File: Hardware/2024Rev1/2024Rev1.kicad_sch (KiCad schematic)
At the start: 87 parts, among them J7 RJ45_LED_Shielded, Q2 BSS138, Q3 BSS138, Q5 BSS138, Q6 SPD30P06PGBTMA1, Q7 BSS138, U2 Opamp_Dual, U3 Teensy4.1_DEV-16771, U4 Opamp_Dual, U5 Opamp_Dual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

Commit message: rearranged flags
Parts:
- removed Conn2: AndersonPP, MRDT_Connectors:Square_Anderson_2_V_Side_By_Side, symbol MRDT_Connectors:AndersonPP
- removed D8: Green, LED_SMD:LED_0603_1608Metric_Pad1.05x0.95mm_HandSolder, symbol Device:LED
- removed R49: 3K, Resistor_SMD:R_0603_1608Metric_Pad0.98x0.95mm_HandSolder, symbol Device:R
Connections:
- net Gate is gone; now on net Cell4-SENSE: U3.41 (A17)
- net Buzzer-Teensy: now also U3.4 (BCLK2); no longer U3.25 (A11)
- net CURRENT_SENSE: now also U3.21 (A7); no longer U3.27 (A13)
- net Cell1-SENSE: now also U3.17 (A3); no longer U3.14 (A0)
- net Cell2-SENSE: now also U3.18 (A4); no longer U3.15 (A1)
- net Cell3-SENSE: now also U3.40 (A16); no longer U3.16 (A2)
- net Cell4-SENSE: no longer U3.17 (A3)
- net Cell5-SENSE: now also U3.38 (A14); no longer U3.18 (A4)
- net Cell6-SENSE: now also U3.39 (A15); no longer U3.19 (A5)
- net Cell7-SENSE: now also U3.25 (A11); no longer U3.20 (A6)
- net Cell8-SENSE: now also U3.24 (A10); no longer U3.21 (A7)
- net ERR_LED: now also U3.34 (RX8); no longer U3.38 (A14)
- net Fan-Teensy: now also U3.23 (A9); no longer U3.26 (A12)
- net GATE: now also U3.33 (MCLK2)
- net LCD_TX: now also U3.20 (A6); no longer U3.1 (TX1)
- net LOGIC_SWITCH_INPUT: now also U3.22 (A8); no longer U3.40 (A16)
- net TempSensor: now also U3.16 (A2); no longer U3.24 (A10)
- no-connect marks 37 -> 35

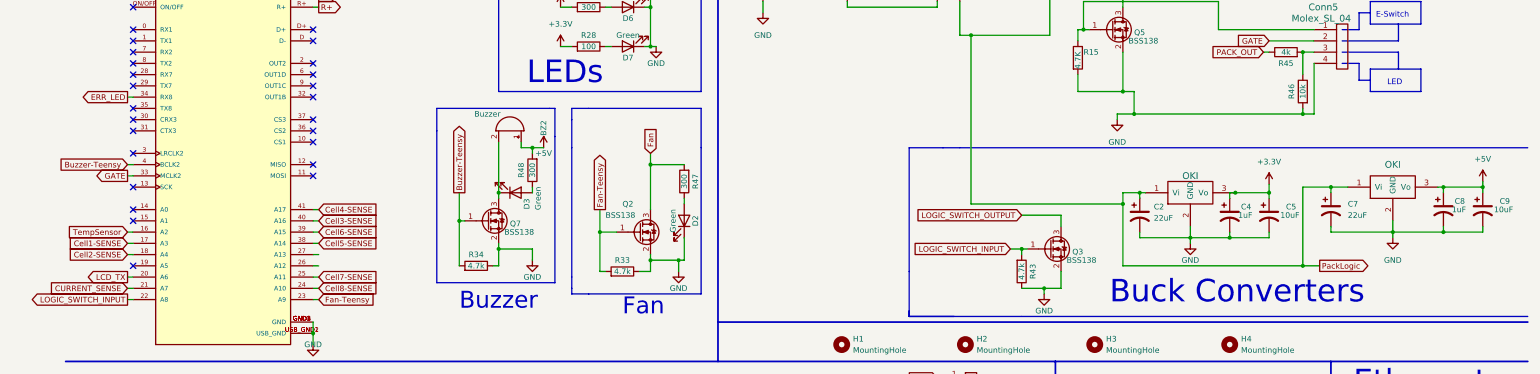
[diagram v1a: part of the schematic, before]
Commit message: polished components placement
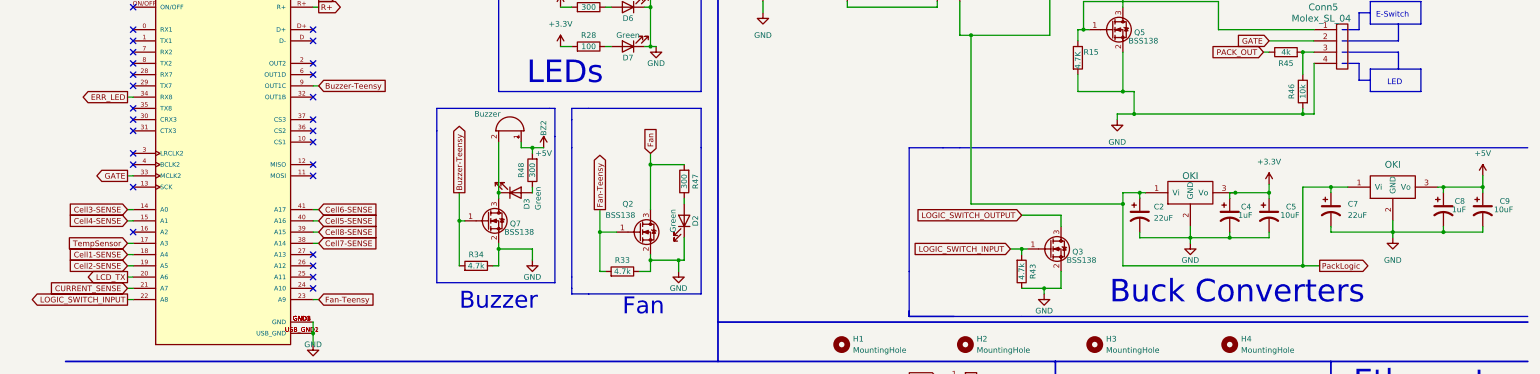
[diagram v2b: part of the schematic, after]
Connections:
- net Buzzer-Teensy: now also U3.9 (OUT1C); no longer U3.4 (BCLK2)
- net Cell1-SENSE: now also U3.18 (A4); no longer U3.17 (A3)
- net Cell2-SENSE: now also U3.19 (A5); no longer U3.18 (A4)
- net Cell3-SENSE: now also U3.14 (A0); no longer U3.40 (A16)
- net Cell4-SENSE: now also U3.15 (A1); no longer U3.41 (A17)
- net Cell5-SENSE: now also U3.40 (A16); no longer U3.38 (A14)
- net Cell6-SENSE: now also U3.41 (A17); no longer U3.39 (A15)
- net Cell7-SENSE: now also U3.38 (A14); no longer U3.25 (A11)
- net Cell8-SENSE: now also U3.39 (A15); no longer U3.24 (A10)
- net TempSensor: now also U3.17 (A3); no longer U3.16 (A2)
- no-connect marks 35 -> 37
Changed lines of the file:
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@@
   (no_connect (at 68.58 64.77))
   (no_connect (at 68.58 59.69))
-  (no_connect (at 68.58 57.15))
   (no_connect (at 68.58 54.61))
   (no_connect (at 68.58 52.07))
@@
   (no_connect (at 27.94 80.01))
   (no_connect (at 68.58 16.51))
+  (no_connect (at 68.58 102.87))
   (no_connect (at 327.66 153.67))
+  (no_connect (at 68.58 95.25))
   (no_connect (at 27.94 46.99))
-  (no_connect (at 27.94 97.79))
-  (no_connect (at 27.94 85.09))
+  (no_connect (at 68.58 100.33))
+  (no_connect (at 27.94 74.93))
   (no_connect (at 68.58 19.05))
+  (no_connect (at 68.58 97.79))
   (no_connect (at 68.58 44.45))
   (no_connect (at 68.58 46.99))
   (no_connect (at 314.96 133.35))
-  (no_connect (at 27.94 87.63))
+  (no_connect (at 27.94 90.17))
   (polyline (pts (xy 300.99 52.07) (xy 304.8 52.07))
     (stroke (width 0) (type default))
   )
+  (wire (pts (xy 26.67 87.63) (xy 27.94 87.63))
+    (stroke (width 0) (type default))
+  )
   (wire (pts (xy 31.75 138.176) (xy 32.004 138.176))
     (stroke (width 0) (type default))
@@
     (stroke (width 0) (type default))
   )
-  (wire (pts (xy 26.67 90.17) (xy 27.94 90.17))
-    (stroke (width 0) (type default))
-  )
   (wire (pts (xy 214.63 45.72) (xy 214.63 38.1))
     (stroke (width 0) (type default))
@@
     (stroke (width 0) (type default))
   )
-  (wire (pts (xy 69.85 100.33) (xy 68.58 100.33))
-    (stroke (width 0) (type default))
-  )
   (wire (pts (xy 26.67 105.41) (xy 27.94 105.41))
     (stroke (width 0) (type default))
@@
     (stroke (width 0) (type default))
   )
-  (wire (pts (xy 26.67 74.93) (xy 27.94 74.93))
-    (stroke (width 0) (type default))
-  )
   (wire (pts (xy 251.46 58.42) (xy 254 58.42))
     (stroke (width 0) (type default))
@@
     (stroke (width 0) (type default))
   )
+  (wire (pts (xy 26.67 85.09) (xy 27.94 85.09))
+    (stroke (width 0) (type default))
+  )
   (polyline (pts (xy 166.624 199.136) (xy 157.734 199.136))
     (stroke (width 0) (type default))
@@
     (stroke (width 0) (type default))
   )
+  (wire (pts (xy 69.85 57.15) (xy 68.58 57.15))
+    (stroke (width 0) (type default))
+  )
   (wire (pts (xy 71.12 165.1) (xy 71.12 168.91))
     (stroke (width 0) (type default))
@@
     (stroke (width 0) (type default))
   )
+  (wire (pts (xy 26.67 97.79) (xy 27.94 97.79))
+    (stroke (width 0) (type default))
+  )
   (polyline (pts (xy 166.624 190.246) (xy 166.624 199.136))
     (stroke (width 0) (type default))
@@
     (stroke (width 0) (type default))
   )
-  (wire (pts (xy 332.74 80.01) (xy 332.74 78.74))
+  (wire (pts (xy 332.74 80.01) (xy 332.74 77.47))
     (stroke (width 0) (type default))
   )
@@
     (stroke (width 0) (type default))
   )
-  (wire (pts (xy 69.85 102.87) (xy 68.58 102.87))
-    (stroke (width 0) (type default))
-  )
   (wire (pts (xy 241.3 44.45) (xy 241.3 46.99))
     (stroke (width 0) (type default))
@@
     (stroke (width 0) (type default))
   )
-  (wire (pts (xy 69.85 95.25) (xy 68.58 95.25))
-    (stroke (width 0) (type default))
-  )
   (wire (pts (xy 137.16 90.17) (xy 133.35 90.17))
     (stroke (width 0) (type default))
@@
     (stroke (width 0) (type default))
   )
-  (wire (pts (xy 69.85 97.79) (xy 68.58 97.79))
-    (stroke (width 0) (type default))
-  )
   (polyline (pts (xy 156.21 62.23) (xy 156.21 71.12))
     (stroke (width 0) (type default))
@@
     (effects (font (size 1.27 1.27)) (justify right bottom))
   )
-  (global_label "Cell4-SENSE" (shape input) (at 69.85 85.09 0) (fields_autoplaced)
-    (effects (font (size 1.27 1.27)) (justify left))
-    (property "Intersheetrefs" "${INTERSHEET_REFS}" (at 85.3536 85.09 0)
-      (effects (font (size 1.27 1.27)) (justify left) hide)
+  (global_label "Cell4-SENSE" (shape input) (at 26.67 87.63 180) (fields_autoplaced)
+    (effects (font (size 1.27 1.27)) (justify right))
+    (property "Intersheetrefs" "${INTERSHEET_REFS}" (at 11.1664 87.63 0)
+      (effects (font (size 1.27 1.27)) (justify right) hide)
     )
   )
@@
     )
   )
-  (global_label "Cell3-SENSE" (shape input) (at 69.85 87.63 0) (fields_autoplaced)
-    (effects (font (size 1.27 1.27)) (justify left))
-    (property "Intersheetrefs" "${INTERSHEET_REFS}" (at 85.3536 87.63 0)
-      (effects (font (size 1.27 1.27)) (justify left) hide)
+  (global_label "Cell3-SENSE" (shape input) (at 26.67 85.09 180) (fields_autoplaced)
+    (effects (font (size 1.27 1.27)) (justify right))
+    (property "Intersheetrefs" "${INTERSHEET_REFS}" (at 11.1664 85.09 0)
+      (effects (font (size 1.27 1.27)) (justify right) hide)
     )
   )
@@
     )
   )
-  (global_label "Cell6-SENSE" (shape input) (at 69.85 90.17 0) (fields_autoplaced)
+  (global_label "Cell6-SENSE" (shape input) (at 69.85 85.09 0) (fields_autoplaced)
     (effects (font (size 1.27 1.27)) (justify left))
-    (property "Intersheetrefs" "${INTERSHEET_REFS}" (at 85.3536 90.17 0)
+    (property "Intersheetrefs" "${INTERSHEET_REFS}" (at 85.3536 85.09 0)
       (effects (font (size 1.27 1.27)) (justify left) hide)
     )
@@
     )
   )
-  (global_label "Cell1-SENSE" (shape input) (at 26.67 92.71 180) (fields_autoplaced)
+  (global_label "Cell1-SENSE" (shape input) (at 26.67 95.25 180) (fields_autoplaced)
     (effects (font (size 1.27 1.27)) (justify right))
-    (property "Intersheetrefs" "${INTERSHEET_REFS}" (at 11.1664 92.71 0)
+    (property "Intersheetrefs" "${INTERSHEET_REFS}" (at 11.1664 95.25 0)
       (effects (font (size 1.27 1.27)) (justify right) hide)
     )
@@
     )
   )
-  (global_label "Cell7-SENSE" (shape input) (at 69.85 100.33 0) (fields_autoplaced)
+  (global_label "Cell7-SENSE" (shape input) (at 69.85 92.71 0) (fields_autoplaced)
     (effects (font (size 1.27 1.27)) (justify left))
-    (property "Intersheetrefs" "${INTERSHEET_REFS}" (at 85.3536 100.33 0)
+    (property "Intersheetrefs" "${INTERSHEET_REFS}" (at 85.3536 92.71 0)
       (effects (font (size 1.27 1.27)) (justify left) hide)
     )
   )
-  (global_label "TempSensor" (shape input) (at 26.67 90.17 180) (fields_autoplaced)
+  (global_label "TempSensor" (shape input) (at 26.67 92.71 180) (fields_autoplaced)
     (effects (font (size 1.27 1.27)) (justify right))
-    (property "Intersheetrefs" "${INTERSHEET_REFS}" (at 12.3759 90.17 0)
+    (property "Intersheetrefs" "${INTERSHEET_REFS}" (at 12.3759 92.71 0)
       (effects (font (size 1.27 1.27)) (justify right) hide)
     )
@@
     )
   )
-  (global_label "Buzzer-Teensy" (shape input) (at 26.67 74.93 180) (fields_autoplaced)
-    (effects (font (size 1.27 1.27)) (justify right))
-    (property "Intersheetrefs" "${INTERSHEET_REFS}" (at 9.4729 74.93 0)
-      (effects (font (size 1.27 1.27)) (justify right) hide)
+  (global_label "Buzzer-Teensy" (shape input) (at 69.85 57.15 0) (fields_autoplaced)
+    (effects (font (size 1.27 1.27)) (justify left))
+    (property "Intersheetrefs" "${INTERSHEET_REFS}" (at 87.0471 57.15 0)
+      (effects (font (size 1.27 1.27)) (justify left) hide)
     )
   )
@@
     )
   )
-  (global_label "Cell2-SENSE" (shape input) (at 26.67 95.25 180) (fields_autoplaced)
+  (global_label "Cell2-SENSE" (shape input) (at 26.67 97.79 180) (fields_autoplaced)
     (effects (font (size 1.27 1.27)) (justify right))
-    (property "Intersheetrefs" "${INTERSHEET_REFS}" (at 11.1664 95.25 0)
+    (property "Intersheetrefs" "${INTERSHEET_REFS}" (at 11.1664 97.79 0)
       (effects (font (size 1.27 1.27)) (justify right) hide)
     )
@@
     )
   )
-  (global_label "Cell8-SENSE" (shape input) (at 69.85 102.87 0) (fields_autoplaced)
+  (global_label "Cell8-SENSE" (shape input) (at 69.85 90.17 0) (fields_autoplaced)
     (effects (font (size 1.27 1.27)) (justify left))
-    (property "Intersheetrefs" "${INTERSHEET_REFS}" (at 85.3536 102.87 0)
+    (property "Intersheetrefs" "${INTERSHEET_REFS}" (at 85.3536 90.17 0)
       (effects (font (size 1.27 1.27)) (justify left) hide)
     )
@@
     )
   )
-  (global_label "Cell5-SENSE" (shape input) (at 69.85 92.71 0) (fields_autoplaced)
+  (global_label "Cell5-SENSE" (shape input) (at 69.85 87.63 0) (fields_autoplaced)
     (effects (font (size 1.27 1.27)) (justify left))
-    (property "Intersheetrefs" "${INTERSHEET_REFS}" (at 85.3536 92.71 0)
+    (property "Intersheetrefs" "${INTERSHEET_REFS}" (at 85.3536 87.63 0)
       (effects (font (size 1.27 1.27)) (justify left) hide)
     )
@@
     )
   )
-  (symbol (lib_id "power:+5V") (at 332.74 78.74 0) (unit 1)
+  (symbol (lib_id "power:+5V") (at 332.74 77.47 0) (unit 1)
     (in_bom yes) (on_board yes) (dnp no) (fields_autoplaced)
-    (property "Reference" "#PWR041" (at 332.74 82.55 0)
+    (property "Reference" "#PWR041" (at 332.74 81.28 0)
       (effects (font (size 1.27 1.27)) hide)
     )
-    (property "Value" "+5V" (at 332.74 73.66 0)
+    (property "Value" "+5V" (at 332.74 72.39 0)
       (effects (font (size 1.27 1.27)))
     )
-    (property "Footprint" "" (at 332.74 78.74 0)
+    (property "Footprint" "" (at 332.74 77.47 0)
       (effects (font (size 1.27 1.27)) hide)
     )
-    (property "Datasheet" "" (at 332.74 78.74 0)
+    (property "Datasheet" "" (at 332.74 77.47 0)
       (effects (font (size 1.27 1.27)) hide)
     )

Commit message: did traces
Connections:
- net Buzzer-Teensy: now also U3.12 (MISO); no longer U3.9 (OUT1C)
- net ERR_LED: now also U3.35 (TX8); no longer U3.34 (RX8)
- net cell2: now also Conn3.3; no longer Conn3.2
- net cell3: now also Conn3.2; no longer Conn3.3
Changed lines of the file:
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@@
   (no_connect (at 312.42 133.35))
   (no_connect (at 68.58 77.47))
-  (no_connect (at 68.58 74.93))
   (no_connect (at 27.94 44.45))
   (no_connect (at 27.94 49.53))
@@
   (no_connect (at 27.94 54.61))
   (no_connect (at 27.94 57.15))
-  (no_connect (at 27.94 62.23))
   (no_connect (at 27.94 64.77))
   (no_connect (at 68.58 69.85))
@@
   (no_connect (at 68.58 102.87))
   (no_connect (at 327.66 153.67))
+  (no_connect (at 27.94 59.69))
   (no_connect (at 68.58 95.25))
   (no_connect (at 27.94 46.99))
+  (no_connect (at 68.58 57.15))
   (no_connect (at 68.58 100.33))
   (no_connect (at 27.94 74.93))
@@
     (stroke (width 0) (type default))
   )
-  (wire (pts (xy 26.67 59.69) (xy 27.94 59.69))
-    (stroke (width 0) (type default))
-  )
   (wire (pts (xy 332.74 80.01) (xy 332.74 81.28))
     (stroke (width 0) (type default))
@@
   )
   (wire (pts (xy 110.49 173.99) (xy 110.49 172.72))
+    (stroke (width 0) (type default))
+  )
+  (wire (pts (xy 69.85 74.93) (xy 68.58 74.93))
     (stroke (width 0) (type default))
   )
@@
     (stroke (width 0) (type default))
   )
-  (wire (pts (xy 69.85 57.15) (xy 68.58 57.15))
-    (stroke (width 0) (type default))
-  )
   (wire (pts (xy 71.12 165.1) (xy 71.12 168.91))
     (stroke (width 0) (type default))
@@
     )
   )
-  (global_label "Buzzer-Teensy" (shape input) (at 69.85 57.15 0) (fields_autoplaced)
-    (effects (font (size 1.27 1.27)) (justify left))
-    (property "Intersheetrefs" "${INTERSHEET_REFS}" (at 87.0471 57.15 0)
+  (global_label "Buzzer-Teensy" (shape input) (at 69.85 74.93 0) (fields_autoplaced)
+    (effects (font (size 1.27 1.27)) (justify left))
+    (property "Intersheetrefs" "${INTERSHEET_REFS}" (at 87.0471 74.93 0)
       (effects (font (size 1.27 1.27)) (justify left) hide)
     )
@@
     )
   )
-  (global_label "cell2" (shape input) (at 209.55 125.73 180) (fields_autoplaced)
+  (global_label "cell2" (shape input) (at 209.55 128.27 180) (fields_autoplaced)
+    (effects (font (size 1.27 1.27)) (justify right))
+    (property "Intersheetrefs" "${INTERSHEET_REFS}" (at 201.8477 128.27 0)
+      (effects (font (size 1.27 1.27)) (justify right) hide)
+    )
+  )
+  (global_label "ERR_LED" (shape output) (at 27.94 62.23 180) (fields_autoplaced)
+    (effects (font (size 1.27 1.27)) (justify right))
+    (property "Intersheetrefs" "${INTERSHEET_REFS}" (at 16.8511 62.23 0)
+      (effects (font (size 1.27 1.27)) (justify right) hide)
+    )
+  )
+  (global_label "PACK_OUT" (shape input) (at 283.21 49.53 180) (fields_autoplaced)
+    (effects (font (size 1.27 1.27)) (justify right))
+    (property "Intersheetrefs" "${INTERSHEET_REFS}" (at 271.3021 49.4506 0)
+      (effects (font (size 1.27 1.27)) (justify right) hide)
+    )
+  )
+  (global_label "Cell2-SENSE" (shape input) (at 26.67 97.79 180) (fields_autoplaced)
+    (effects (font (size 1.27 1.27)) (justify right))
+    (property "Intersheetrefs" "${INTERSHEET_REFS}" (at 11.1664 97.79 0)
+      (effects (font (size 1.27 1.27)) (justify right) hide)
+    )
+  )
+  (global_label "cell1" (shape input) (at 173.99 184.15 270) (fields_autoplaced)
+    (effects (font (size 1.27 1.27)) (justify right))
+    (property "Intersheetrefs" "${INTERSHEET_REFS}" (at 174.0694 191.2802 90)
+      (effects (font (size 1.27 1.27)) (justify right) hide)
+    )
+  )
+  (global_label "TempSensor" (shape output) (at 264.16 153.67 180) (fields_autoplaced)
+    (effects (font (size 1.27 1.27)) (justify right))
+    (property "Intersheetrefs" "${INTERSHEET_REFS}" (at 249.8659 153.67 0)
+      (effects (font (size 1.27 1.27)) (justify right) hide)
+    )
+  )
+  (global_label "PackLogic" (shape input) (at 167.64 137.16 90) (fields_autoplaced)
+    (effects (font (size 1.27 1.27)) (justify left))
+    (property "Intersheetrefs" "${INTERSHEET_REFS}" (at 167.5606 125.1917 90)
+      (effects (font (size 1.27 1.27)) (justify left) hide)
+    )
+  )
+  (global_label "ERR_LED" (shape input) (at 125.73 21.59 180) (fields_autoplaced)
+    (effects (font (size 1.27 1.27)) (justify right))
+    (property "Intersheetrefs" "${INTERSHEET_REFS}" (at 115.2131 21.6694 0)
+      (effects (font (size 1.27 1.27)) (justify right) hide)
+    )
+  )
+  (global_label "cell3" (shape input) (at 209.55 125.73 180) (fields_autoplaced)
     (effects (font (size 1.27 1.27)) (justify right))
     (property "Intersheetrefs" "${INTERSHEET_REFS}" (at 201.8477 125.73 0)
       (effects (font (size 1.27 1.27)) (justify right) hide)
     )
-  )
-  (global_label "ERR_LED" (shape output) (at 26.67 59.69 180) (fields_autoplaced)
-    (effects (font (size 1.27 1.27)) (justify right))
-    (property "Intersheetrefs" "${INTERSHEET_REFS}" (at 15.5811 59.69 0)
-      (effects (font (size 1.27 1.27)) (justify right) hide)
-    )
-  )
-  (global_label "PACK_OUT" (shape input) (at 283.21 49.53 180) (fields_autoplaced)
-    (effects (font (size 1.27 1.27)) (justify right))
-    (property "Intersheetrefs" "${INTERSHEET_REFS}" (at 271.3021 49.4506 0)
-      (effects (font (size 1.27 1.27)) (justify right) hide)
-    )
-  )
-  (global_label "Cell2-SENSE" (shape input) (at 26.67 97.79 180) (fields_autoplaced)
-    (effects (font (size 1.27 1.27)) (justify right))
-    (property "Intersheetrefs" "${INTERSHEET_REFS}" (at 11.1664 97.79 0)
-      (effects (font (size 1.27 1.27)) (justify right) hide)
-    )
-  )
-  (global_label "cell1" (shape input) (at 173.99 184.15 270) (fields_autoplaced)
-    (effects (font (size 1.27 1.27)) (justify right))
-    (property "Intersheetrefs" "${INTERSHEET_REFS}" (at 174.0694 191.2802 90)
-      (effects (font (size 1.27 1.27)) (justify right) hide)
-    )
-  )
-  (global_label "TempSensor" (shape output) (at 264.16 153.67 180) (fields_autoplaced)
-    (effects (font (size 1.27 1.27)) (justify right))
-    (property "Intersheetrefs" "${INTERSHEET_REFS}" (at 249.8659 153.67 0)
-      (effects (font (size 1.27 1.27)) (justify right) hide)
-    )
-  )
-  (global_label "PackLogic" (shape input) (at 167.64 137.16 90) (fields_autoplaced)
-    (effects (font (size 1.27 1.27)) (justify left))
-    (property "Intersheetrefs" "${INTERSHEET_REFS}" (at 167.5606 125.1917 90)
-      (effects (font (size 1.27 1.27)) (justify left) hide)
-    )
-  )
-  (global_label "ERR_LED" (shape input) (at 125.73 21.59 180) (fields_autoplaced)
-    (effects (font (size 1.27 1.27)) (justify right))
-    (property "Intersheetrefs" "${INTERSHEET_REFS}" (at 115.2131 21.6694 0)
-      (effects (font (size 1.27 1.27)) (justify right) hide)
-    )
-  )
-  (global_label "cell3" (shape input) (at 209.55 128.27 180) (fields_autoplaced)
-    (effects (font (size 1.27 1.27)) (justify right))
-    (property "Intersheetrefs" "${INTERSHEET_REFS}" (at 201.8477 128.27 0)
-      (effects (font (size 1.27 1.27)) (justify right) hide)
-    )

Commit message: rearranged components and flags. also started on some traces
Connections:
- net Buzzer-Teensy: now also U3.34 (RX8); no longer U3.12 (MISO)
- net CURRENT_SENSE: now also U3.24 (A10); no longer U3.21 (A7)
- net ERR_LED: now also U3.33 (MCLK2); no longer U3.35 (TX8)
- net GATE: now also U3.35 (TX8); no longer U3.33 (MCLK2)
- net cell4: now also Conn3.5; no longer Conn3.4
- net cell5: now also Conn3.4; no longer Conn3.5
- net cell6: now also Conn3.7; no longer Conn3.6
- net cell7: now also Conn3.6; no longer Conn3.7

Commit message: did more traces
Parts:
- Q6: footprint Package_TO_SOT_SMD:TO-252-2 -> Package_TO_SOT_SMD:TO-263-7_TabPin4
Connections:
- net Cell7-SENSE: now also U3.39 (A15); no longer U3.38 (A14)
- net Cell8-SENSE: now also U3.38 (A14); no longer U3.39 (A15)
